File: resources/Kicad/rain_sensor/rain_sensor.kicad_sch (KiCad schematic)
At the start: 10 parts, among them U1 TP4056 18650 Battery Charger, U4 MCP1702-3302E, U5 XIAO-ESP32-C3-DIP

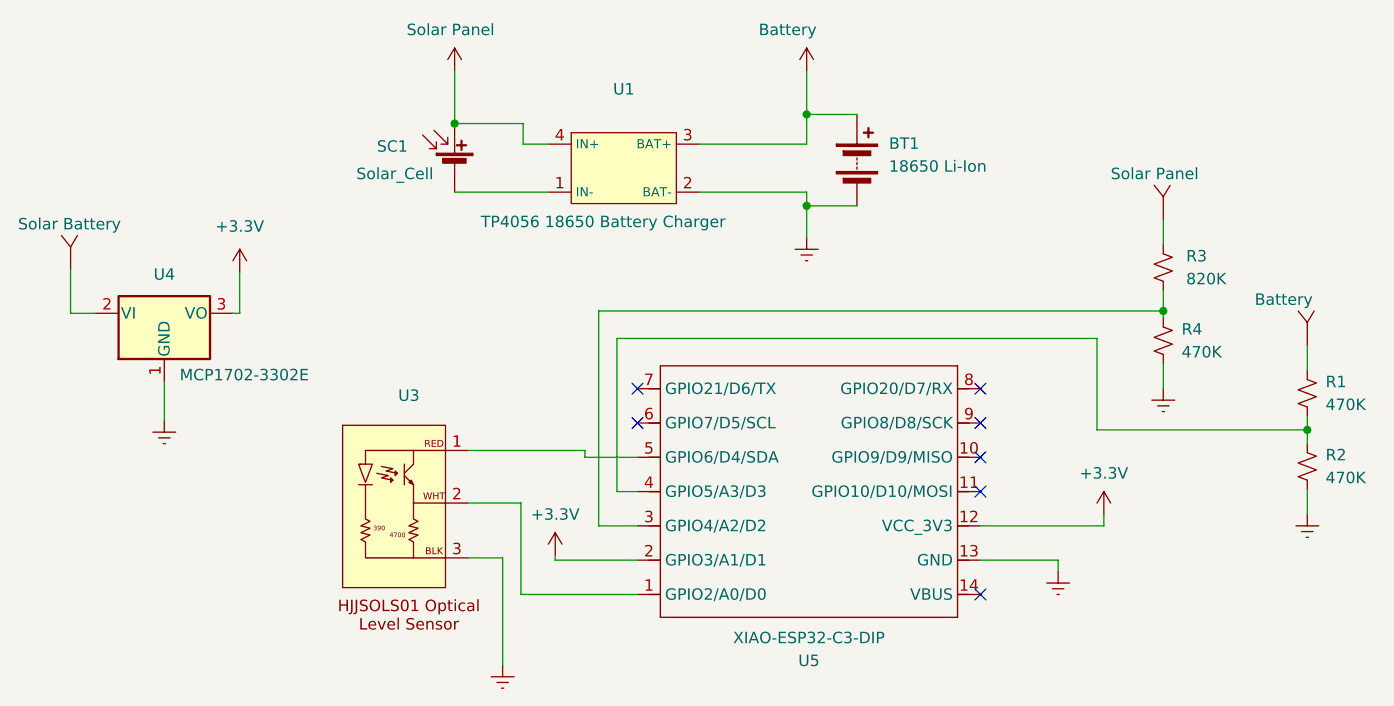
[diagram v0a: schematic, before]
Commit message: Fixed some calculations and reduced the code base to espressif32@5.4.0 to enable use of A3 port
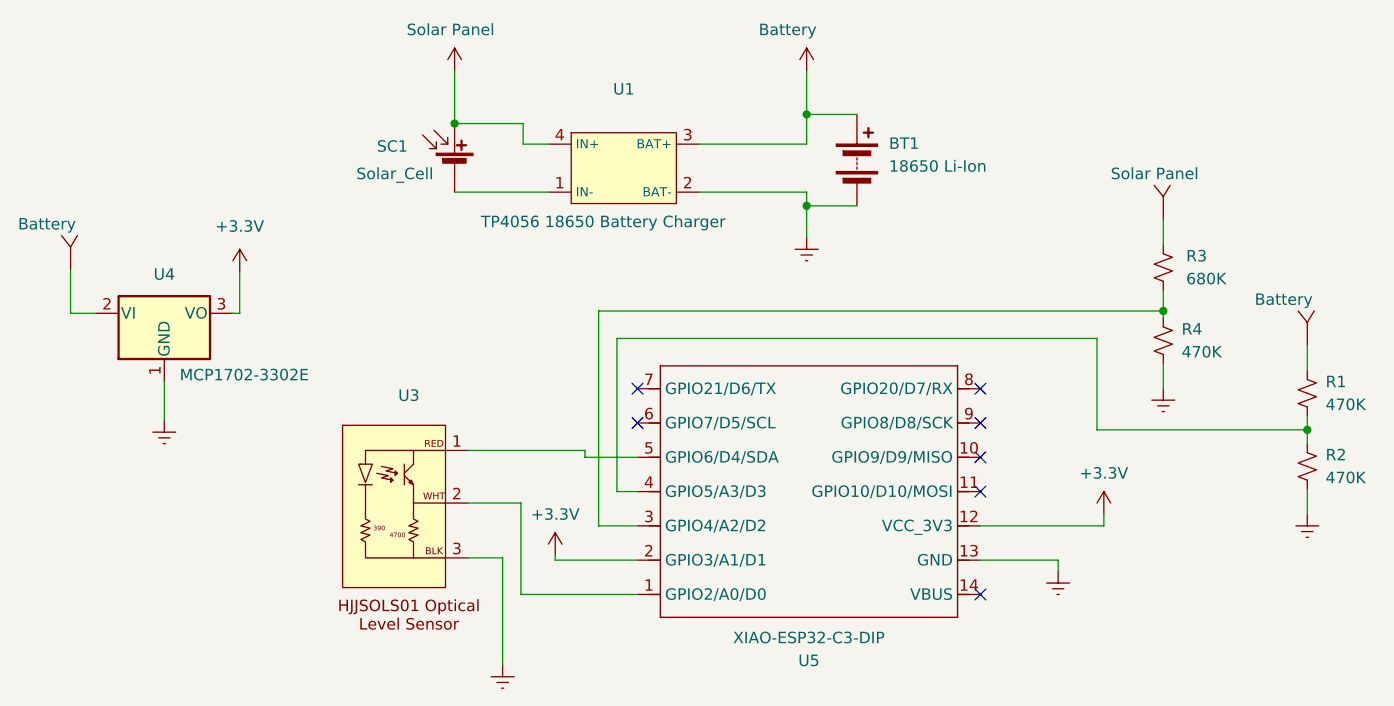
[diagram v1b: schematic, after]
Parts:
- R3: value 820K -> 680K
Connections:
- net Solar Battery is gone; now on net Battery: U4.2 (VI)
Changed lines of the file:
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@@
 			)
 		)
-		(property "Value" "820K"
+		(property "Value" "680K"
 			(at 208.28 87.1219 0)
 			(effects
@@
 			)
 		)
-		(property "Value" "Solar Battery"
+		(property "Value" "Battery"
 			(at 78.486 81.026 0)
 			(effects
